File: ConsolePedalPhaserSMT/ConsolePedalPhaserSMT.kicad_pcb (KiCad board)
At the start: 2 copper layers, 100 x 60 mm, 56 parts, among them J1 Conn_02x25_Counter_Clockwise, Q1 2N5457, Q2 2N5457, Q3 2N5457, Q4 2N5457, Q5 2N3906, U1 TL072, U2 TL072, U3 TL072

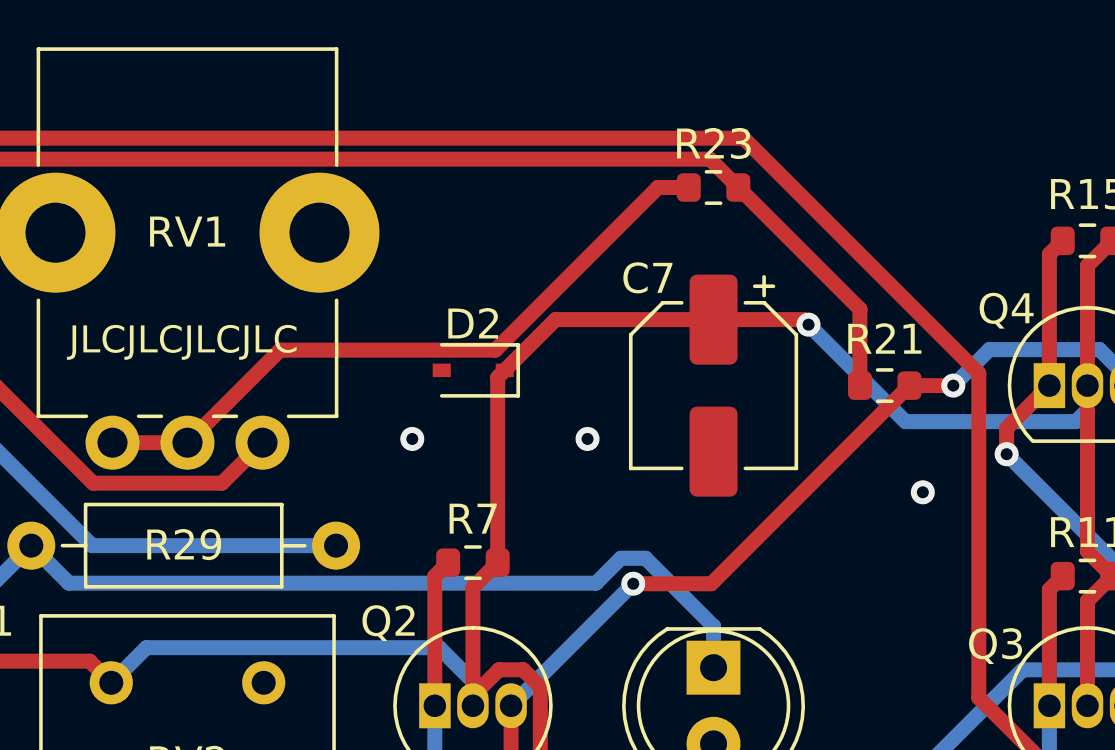
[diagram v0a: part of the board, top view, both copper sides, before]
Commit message: Finalized board and created assembly files
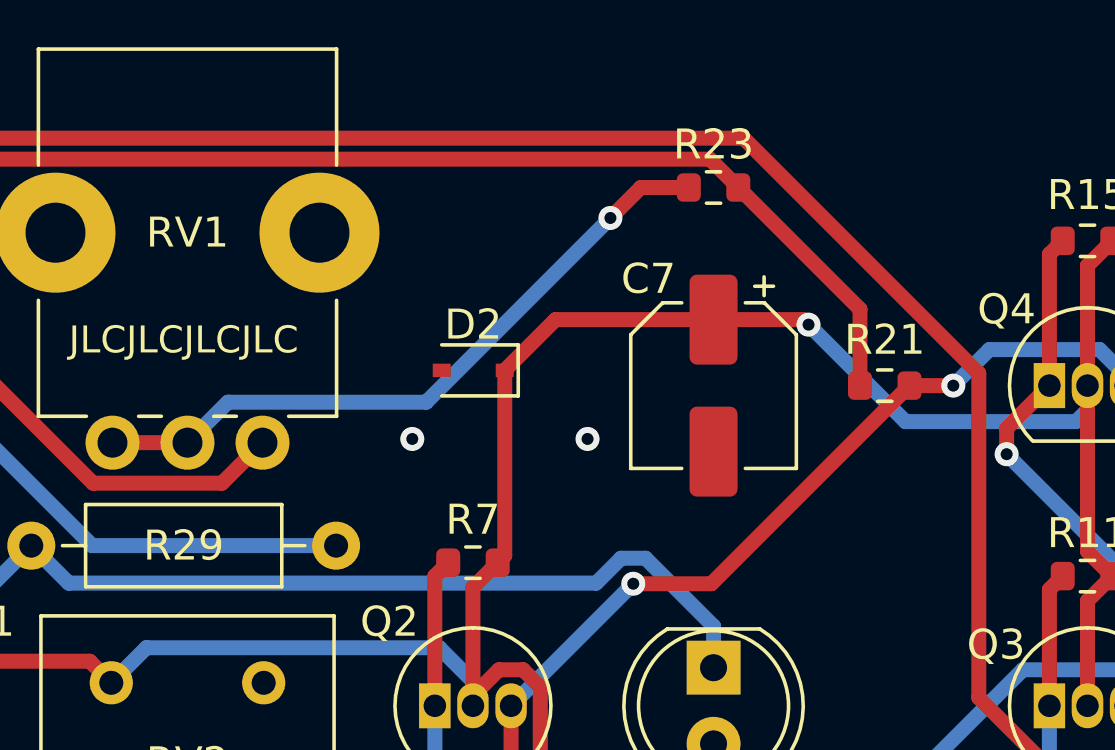
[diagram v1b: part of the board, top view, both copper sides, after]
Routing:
- net Net-(R23-Pad1): vias 0 -> 1
- net GND: vias 15 -> 14
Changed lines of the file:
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@@
     (thickness 1.2)
     (drawings 33)
-    (tracks 398)
+    (tracks 399)
     (zones 0)
     (modules 56)
@@
       (drillshape 0)
       (scaleselection 1)
-      (outputdirectory "Gerbers/"))
+      (outputdirectory "assembly/"))
   )
   (net 0 "")
@@
   (via (at 112.776 99.568) (size 0.8) (drill 0.4) (layers F.Cu B.Cu) (net 1))
   (via (at 126.492 100.076) (size 0.8) (drill 0.4) (layers F.Cu B.Cu) (net 1))
-  (via (at 157.226 89.154) (size 0.8) (drill 0.4) (layers F.Cu B.Cu) (net 1))
   (segment (start 115.25 126) (end 115.25 121.454) (width 0.5) (layer F.Cu) (net 2) (status 10))
   (via (at 115.25 121.454) (size 0.8) (drill 0.4) (layers F.Cu B.Cu) (net 2))
@@
   (segment (start 144.982 83.398) (end 143.29 85.09) (width 0.5) (layer F.Cu) (net 16))
   (segment (start 150.25 83.398) (end 144.982 83.398) (width 0.5) (layer F.Cu) (net 16))
-  (segment (start 143.055 85.325) (end 143.29 85.09) (width 0.5) (layer F.Cu) (net 16))
-  (segment (start 143.055 91.5) (end 143.055 85.325) (width 0.5) (layer F.Cu) (net 16))
   (segment (start 123.27 92.325) (end 123.27 96.27) (width 0.5) (layer F.Cu) (net 16))
   (segment (start 124.095 91.5) (end 123.27 92.325) (width 0.5) (layer F.Cu) (net 16))
@@
   (segment (start 122.495 102.27) (end 120.742 102.27) (width 0.5) (layer F.Cu) (net 16))
   (segment (start 120.65 102.362) (end 109.728 102.362) (width 0.5) (layer B.Cu) (net 16))
+  (segment (start 143.29 91.265) (end 143.055 91.5) (width 0.5) (layer F.Cu) (net 16))
+  (segment (start 143.29 85.09) (end 143.29 91.265) (width 0.5) (layer F.Cu) (net 16))
   (segment (start 164.39001 86.00301) (end 163.985 85.598) (width 0.5) (layer F.Cu) (net 17))
   (segment (start 164.39001 95.86499) (end 164.39001 86.00301) (width 0.5) (layer F.Cu) (net 17))
@@
   (segment (start 132.715 100.584) (end 141.405 100.584) (width 0.5) (layer F.Cu) (net 29))
   (segment (start 130.215 87.5) (end 132.715 87.5) (width 0.5) (layer F.Cu) (net 30))
-  (segment (start 148.396038 78.994) (end 149.425 78.994) (width 0.5) (layer F.Cu) (net 30))
-  (segment (start 142.975039 84.414999) (end 148.396038 78.994) (width 0.5) (layer F.Cu) (net 30))
-  (segment (start 135.800001 84.414999) (end 142.975039 84.414999) (width 0.5) (layer F.Cu) (net 30))
-  (segment (start 132.715 87.5) (end 135.800001 84.414999) (width 0.5) (layer F.Cu) (net 30))
+  (via (at 146.812 80.01) (size 0.8) (drill 0.4) (layers F.Cu B.Cu) (net 30))
+  (segment (start 147.828 78.994) (end 146.812 80.01) (width 0.5) (layer F.Cu) (net 30))
+  (segment (start 149.425 78.994) (end 147.828 78.994) (width 0.5) (layer F.Cu) (net 30))
+  (segment (start 134.065001 86.149999) (end 132.715 87.5) (width 0.5) (layer B.Cu) (net 30))
+  (segment (start 140.672001 86.149999) (end 134.065001 86.149999) (width 0.5) (layer B.Cu) (net 30))
+  (segment (start 146.812 80.01) (end 140.672001 86.149999) (width 0.5) (layer B.Cu) (net 30))
   (segment (start 105.237 104.648) (end 105.19 104.601) (width 0.5) (layer F.Cu) (net 31))
   (segment (start 108.141 104.648) (end 105.237 104.648) (width 0.5) (layer F.Cu) (net 31))

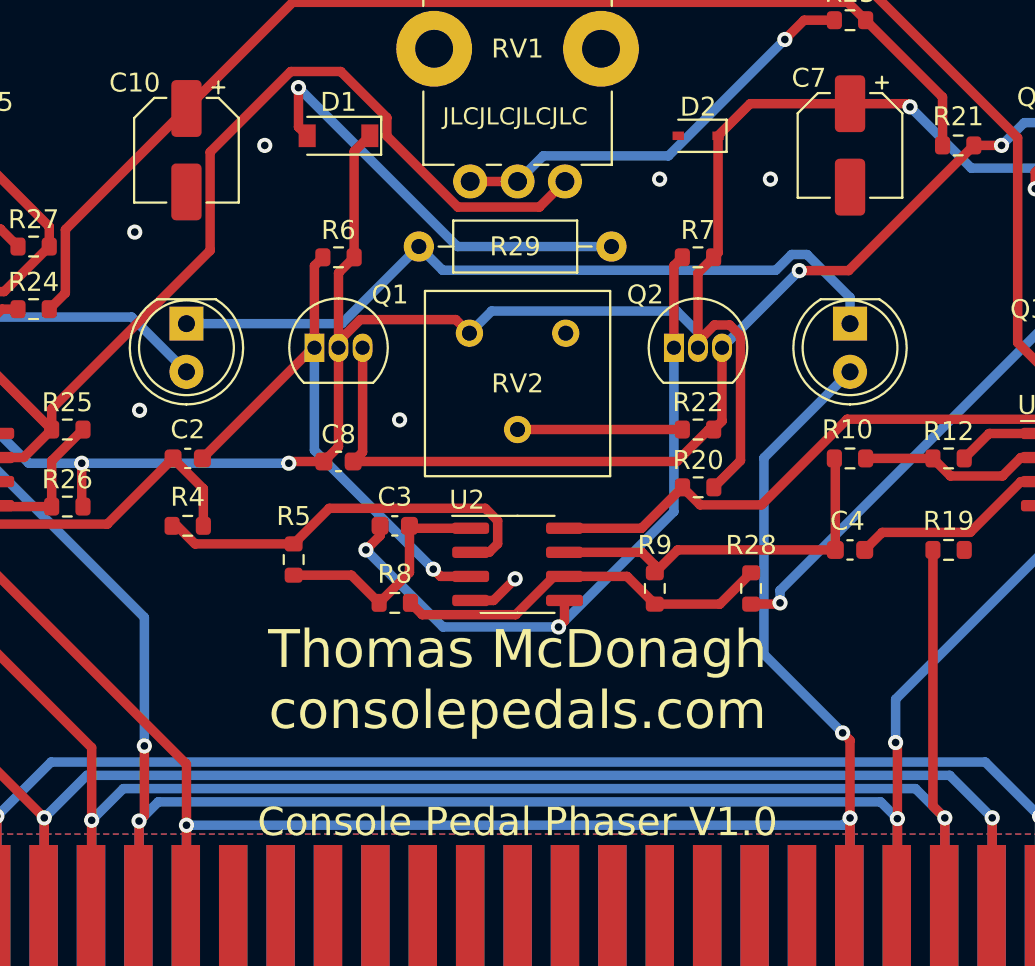
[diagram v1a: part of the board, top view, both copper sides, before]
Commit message: Fixed rotation issues
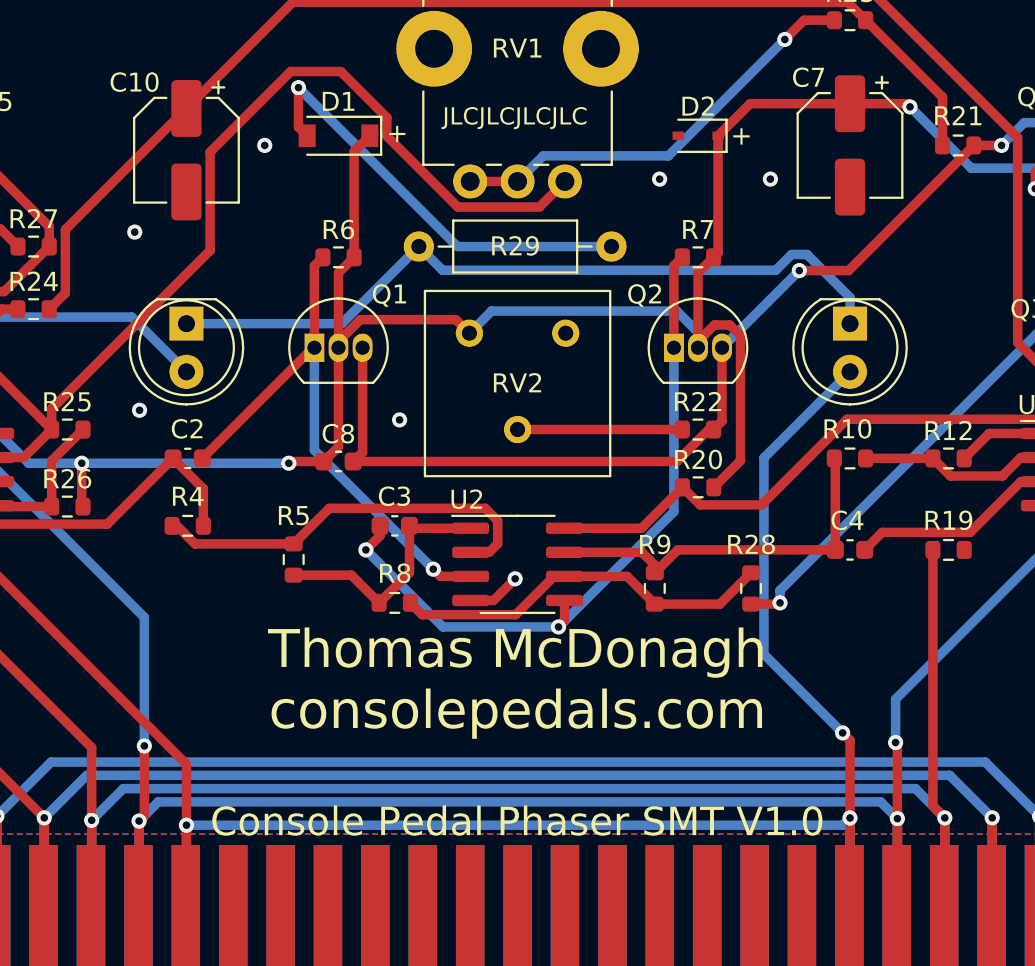
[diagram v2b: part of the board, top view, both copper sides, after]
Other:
- board text added: "+"
- board text added: "Console Pedal Phaser SMT V1.0"
- board text removed: "Console Pedal Phaser V1.0"

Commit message: Added image files for logo
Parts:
- added G***: LOGO, libraries:phaserLogo, B.Cu at (132.5, 85.7)
